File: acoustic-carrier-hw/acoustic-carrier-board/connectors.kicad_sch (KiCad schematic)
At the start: 1 part, among them J902 Conn_02x09_Odd_Even

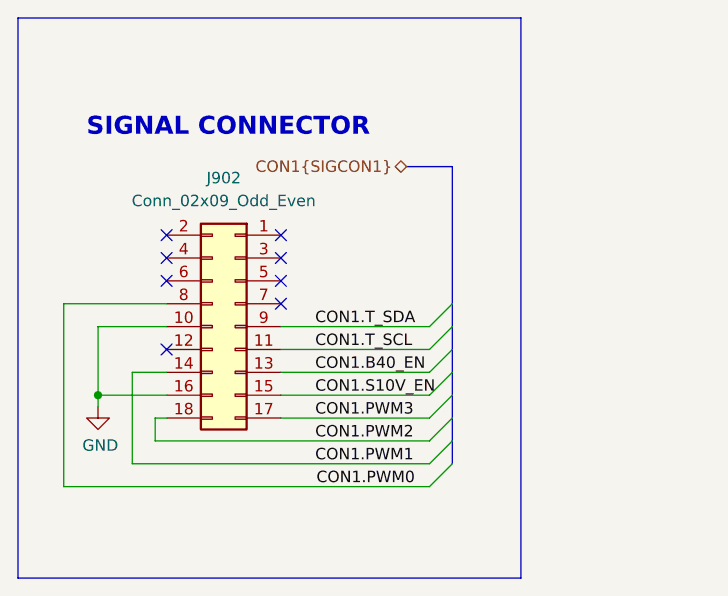
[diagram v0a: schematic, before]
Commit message: [carrier] Change connectors to PMOD, follow specifications, check gappropriate power conenctor
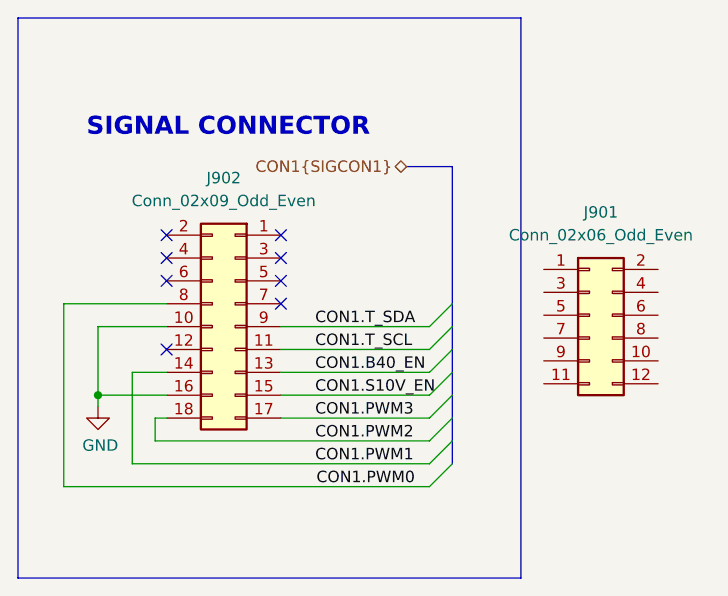
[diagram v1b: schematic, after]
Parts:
- added J901: Conn_02x06_Odd_Even, Connector_PinHeader_2.54mm:PinHeader_2x06_P2.54mm_Horizontal, symbol Connector_Generic:Conn_02x06_Odd_Even
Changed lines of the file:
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@@
+	)
+	(symbol
+		(lib_id "Connector_Generic:Conn_02x06_Odd_Even")
+		(at 83.82 59.69 0)
+		(unit 1)
+		(exclude_from_sim no)
+		(in_bom yes)
+		(on_board yes)
+		(dnp no)
+		(fields_autoplaced yes)
+		(property "Reference" "J901"
+			(at 85.09 48.26 0)
+			(effects
+				(font
+					(size 1.27 1.27)
+				)
+			)
+		)
+		(property "Value" "Conn_02x06_Odd_Even"
+			(at 85.09 50.8 0)
+			(effects
+				(font
+					(size 1.27 1.27)
+				)
+			)
+		)
+		(property "Footprint" "Connector_PinHeader_2.54mm:PinHeader_2x06_P2.54mm_Horizontal"
+			(at 83.82 59.69 0)
+			(effects
+				(font
+					(size 1.27 1.27)
+				)
+				(hide yes)
+			)
+		)
+		(property "Datasheet" "~"
+			(at 83.82 59.69 0)
+			(effects
+				(font
+					(size 1.27 1.27)
+				)
+				(hide yes)
+			)
+		)
+		(property "Description" "Generic connector, double row, 02x06, odd/even pin numbering scheme (row 1 odd numbers, row 2 even numbers), script generated (kicad-library-utils/schlib/autogen/connector/)"
+			(at 83.82 59.69 0)
+			(effects
+				(font
+					(size 1.27 1.27)
+				)
+				(hide yes)
+			)
+		)
+		(pin "11"
+		)
+		(pin "6"
+		)
+		(pin "4"
+		)
+		(pin "7"
+		)
+		(pin "5"
+		)
+		(pin "3"
+		)
+		(pin "2"
+		)
+		(pin "9"
+		)
+		(pin "10"
+		)
+		(pin "12"
+		)
+		(pin "8"
+		)
+		(pin "1"
+		)
+		(instances
+			(project "acoustic-carrier-board"
+				(path "/25b015c9-ab13-4427-b72c-b6f348597100/bc102b0c-2088-41b9-b570-4eb098131c8b"
+					(reference "J901")
+					(unit 1)
+				)
+			)
+		)
 	)
 	(symbol

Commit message: [carrier] Redid routing to PMOD SPI-flash ah (next) add second PMOD-connector and third connector meant for PWM signalling to power board
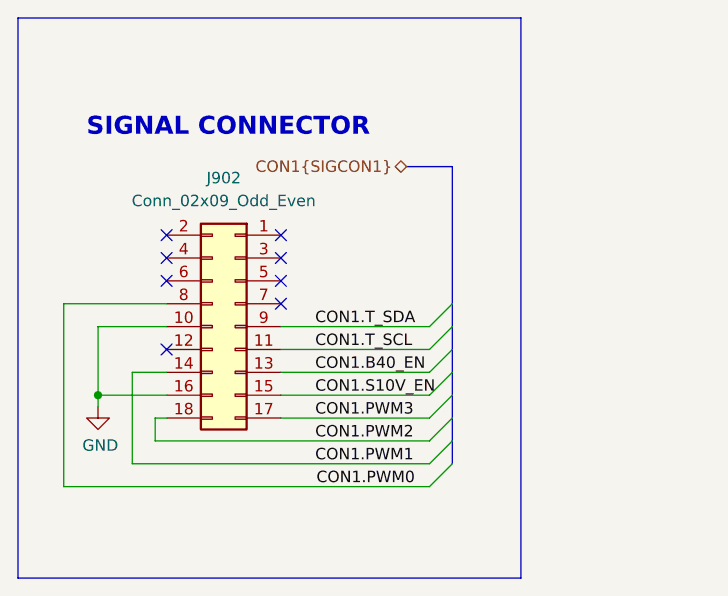
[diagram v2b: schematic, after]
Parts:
- removed J901: Conn_02x06_Odd_Even, Connector_PinHeader_2.54mm:PinHeader_2x06_P2.54mm_Horizontal, symbol Connector_Generic:Conn_02x06_Odd_Even
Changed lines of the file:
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@@
-	)
-	(symbol
-		(lib_id "Connector_Generic:Conn_02x06_Odd_Even")
-		(at 83.82 59.69 0)
-		(unit 1)
-		(exclude_from_sim no)
-		(in_bom yes)
-		(on_board yes)
-		(dnp no)
-		(fields_autoplaced yes)
-		(property "Reference" "J901"
-			(at 85.09 48.26 0)
-			(effects
-				(font
-					(size 1.27 1.27)
-				)
-			)
-		)
-		(property "Value" "Conn_02x06_Odd_Even"
-			(at 85.09 50.8 0)
-			(effects
-				(font
-					(size 1.27 1.27)
-				)
-			)
-		)
-		(property "Footprint" "Connector_PinHeader_2.54mm:PinHeader_2x06_P2.54mm_Horizontal"
-			(at 83.82 59.69 0)
-			(effects
-				(font
-					(size 1.27 1.27)
-				)
-				(hide yes)
-			)
-		)
-		(property "Datasheet" "~"
-			(at 83.82 59.69 0)
-			(effects
-				(font
-					(size 1.27 1.27)
-				)
-				(hide yes)
-			)
-		)
-		(property "Description" "Generic connector, double row, 02x06, odd/even pin numbering scheme (row 1 odd numbers, row 2 even numbers), script generated (kicad-library-utils/schlib/autogen/connector/)"
-			(at 83.82 59.69 0)
-			(effects
-				(font
-					(size 1.27 1.27)
-				)
-				(hide yes)
-			)
-		)
-		(pin "11"
-		)
-		(pin "6"
-		)
-		(pin "4"
-		)
-		(pin "7"
-		)
-		(pin "5"
-		)
-		(pin "3"
-		)
-		(pin "2"
-		)
-		(pin "9"
-		)
-		(pin "10"
-		)
-		(pin "12"
-		)
-		(pin "8"
-		)
-		(pin "1"
-		)
-		(instances
-			(project "acoustic-carrier-board"
-				(path "/25b015c9-ab13-4427-b72c-b6f348597100/bc102b0c-2088-41b9-b570-4eb098131c8b"
-					(reference "J901")
-					(unit 1)
-				)
-			)
-		)
 	)
 	(symbol
